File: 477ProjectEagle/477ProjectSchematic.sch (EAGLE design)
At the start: 66 parts, among them J1 POWER_JACKPTH, Q1 AO4419, X1 22-23-2051, X10 22-23-2041, X2 XRJK-S-01-6-6-0-2G2-NO

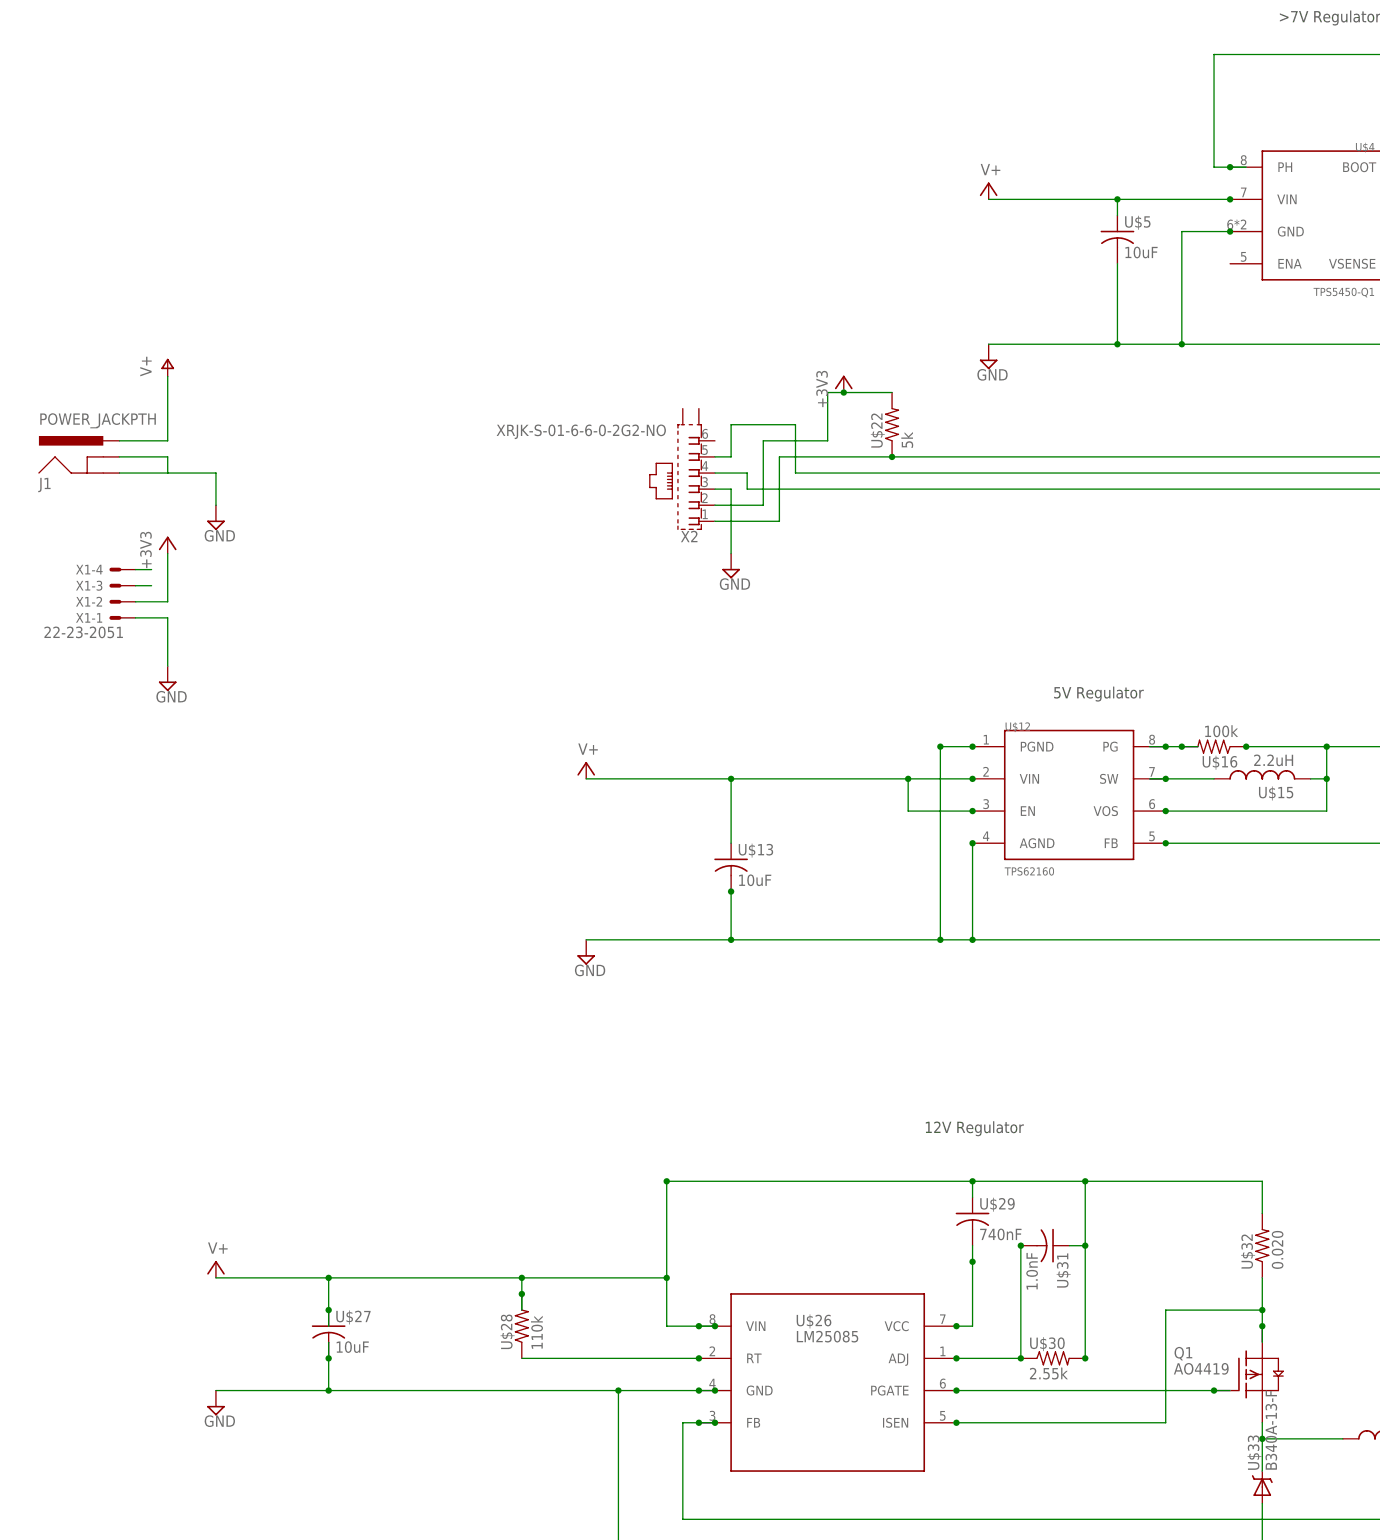
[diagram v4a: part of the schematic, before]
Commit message: started main PCB layout - 12V supply done
Started the PCB layout. Got the 12 volt power supply circuit done. We
only have the Light version of eagle so I couldn't actually make the PCB
the right size.
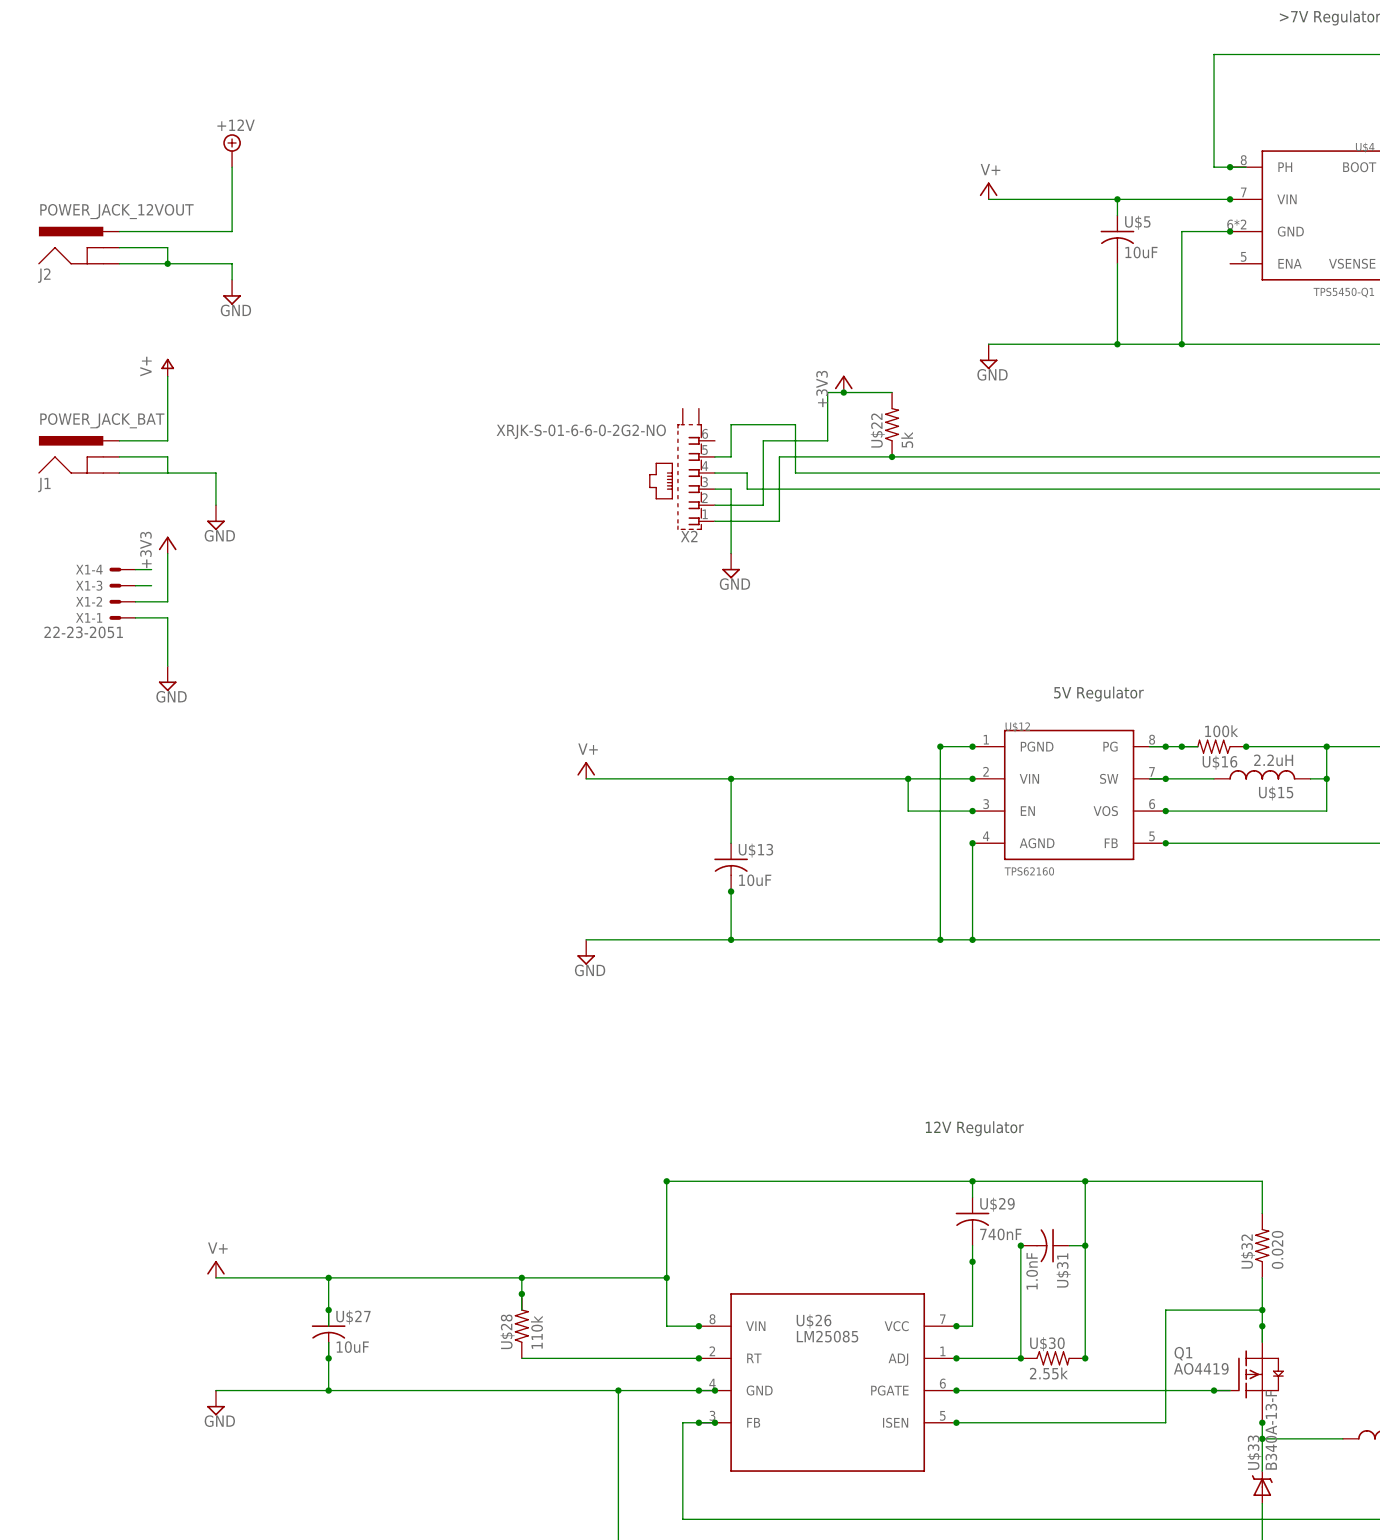
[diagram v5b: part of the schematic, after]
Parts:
- added J2: POWER_JACK_12VOUT, SparkFun-Connectors:POWER_JACKPTH
- J1: value POWER_JACKPTH -> POWER_JACK_BAT
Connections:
- net +12V: now also J2.PWR
- net GND: now also J2.GND, J2.GNDBREAK
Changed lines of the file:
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@@
 <part name="SUPPLY43" library="supply2" deviceset="V+" device=""/>
 <part name="+3V7" library="supply1" deviceset="+3V3" device=""/>
-<part name="J1" library="SparkFun-Connectors" deviceset="POWER_JACK" device="PTH"/>
+<part name="J1" library="SparkFun-Connectors" deviceset="POWER_JACK" device="PTH" value="POWER_JACK_BAT"/>
 <part name="P+1" library="supply1" deviceset="V+" device=""/>
 <part name="SUPPLY44" library="supply2" deviceset="GND" device=""/>
@@
 <part name="U$49" library="MinotaurParts" deviceset="C-US-1206" device="" value="10uF"/>
 <part name="SUPPLY48" library="supply2" deviceset="GND" device=""/>
+<part name="J2" library="SparkFun-Connectors" deviceset="POWER_JACK" device="PTH" value="POWER_JACK_12VOUT"/>
+<part name="SUPPLY49" library="supply2" deviceset="GND" device=""/>
+<part name="SUPPLY50" library="supply2" deviceset="+12V" device=""/>
 </parts>
 <sheets>
@@
 <instance part="U$49" gate="G$1" x="-172.72" y="-83.82"/>
 <instance part="SUPPLY48" gate="GND" x="-152.4" y="-93.98"/>
+<instance part="J2" gate="G$1" x="-436.88" y="73.66"/>
+<instance part="SUPPLY49" gate="GND" x="-416.56" y="71.12"/>
+<instance part="SUPPLY50" gate="+12V" x="-416.56" y="93.98"/>
 </instances>
 <busses>
@@
 <wire x1="-254" y1="-109.22" x2="-241.3" y2="-109.22" width="0.1524" layer="91"/>
 <junction x="-254" y="-109.22"/>
+<junction x="-254" y="-106.68"/>
 </segment>
 </net>
@@
 <junction x="-172.72" y="-88.9"/>
 </segment>
+<segment>
+<pinref part="J2" gate="G$1" pin="GNDBREAK"/>
+<wire x1="-434.34" y1="78.74" x2="-426.72" y2="78.74" width="0.1524" layer="91"/>
+<wire x1="-426.72" y1="78.74" x2="-426.72" y2="76.2" width="0.1524" layer="91"/>
+<pinref part="J2" gate="G$1" pin="GND"/>
+<wire x1="-426.72" y1="76.2" x2="-434.34" y2="76.2" width="0.1524" layer="91"/>
+<wire x1="-426.72" y1="76.2" x2="-416.56" y2="76.2" width="0.1524" layer="91"/>
+<wire x1="-416.56" y1="76.2" x2="-416.56" y2="73.66" width="0.1524" layer="91"/>
+<pinref part="SUPPLY49" gate="GND" pin="GND"/>
+<junction x="-426.72" y="76.2"/>
+</segment>
 </net>
 <net name="N$16" class="0">
@@
 <junction x="-175.26" y="-109.22"/>
 </segment>
+<segment>
+<pinref part="J2" gate="G$1" pin="PWR"/>
+<wire x1="-434.34" y1="81.28" x2="-416.56" y2="81.28" width="0.1524" layer="91"/>
+<wire x1="-416.56" y1="81.28" x2="-416.56" y2="91.44" width="0.1524" layer="91"/>
+<pinref part="SUPPLY50" gate="+12V" pin="+12V"/>
+</segment>
 </net>
 <net name="N$15" class="0">
@@
 <wire x1="-347.98" y1="-83.82" x2="-347.98" y2="-91.44" width="0.1524" layer="91"/>
 <wire x1="-347.98" y1="-91.44" x2="-342.9" y2="-91.44" width="0.1524" layer="91"/>
-<wire x1="-342.9" y1="-91.44" x2="-340.36" y2="-91.44" width="0.1524" layer="91"/>
 <wire x1="-370.84" y1="-88.9" x2="-370.84" y2="-86.36" width="0.1524" layer="91"/>
 <wire x1="-370.84" y1="-86.36" x2="-370.84" y2="-83.82" width="0.1524" layer="91"/>
@@
 <junction x="-281.94" y="-78.74"/>
 <junction x="-281.94" y="-96.52"/>
-<junction x="-340.36" y="-91.44"/>
 <pinref part="U$26" gate="G$1" pin="VIN"/>
-<junction x="-342.9" y="-91.44"/>
 <pinref part="U$27" gate="G$1" pin="1"/>
 <junction x="-401.32" y="-88.9"/>
@@
 <junction x="-401.32" y="-83.82"/>
 <pinref part="SUPPLY43" gate="1" pin="V+"/>
-</segment>
-<segment>
+<junction x="-342.9" y="-91.44"/>
+</segment>
+<segment>

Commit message: More work on main PCB
Fixed some trace sizes on 12V power supply. Fixed some library
components to be the right size (Cout for the 7V power supply). Started
laying out 7V power supply circuit
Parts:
- renumbered U$10 to D1_7, U$11 to COUT7, U$27 to CIN12, U$28 to RT12, U$29 to CVCC12, U$30 to RAJ12, U$31 to CADJ12, U$32 to RSNS12, U$33 to D1_12, U$34 to L1_12, U$38 to COUT12, U$5 to CIN7, U$6 to CBOOT7, U$7 to L1_7
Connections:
- net N$59: now also SV4.8
- net N$68: now also SV4.9
- net N$69: now also SV4.7
- net N$74: now also SV4.2
- net N$75: now also SV4.1

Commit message: Scott from lab -- worked on main PCB
Got all of the power supply circuits hooked up. Need to review them a
little bit more to make sure all traces are large enough etc...The board
is now 4 inches by 5 inches. That seems to be big enough
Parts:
- renumbered U$13 to CIN5, U$14 to COUT5, U$15 to L1_5, U$17 to R1_5, U$18 to R2_5
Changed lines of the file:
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@@
 <part name="D1_7" library="MinotaurParts" deviceset="B340A-13-F" device=""/>
 <part name="U$12" library="MinotaurParts" deviceset="TPS62160" device=""/>
-<part name="U$13" library="MinotaurParts" deviceset="C-US-1206" device="" value="10uF"/>
-<part name="U$14" library="MinotaurParts" deviceset="C-US-1206" device="" value="22uF"/>
+<part name="CIN5" library="MinotaurParts" deviceset="C-US-1206" device="" value="10uF"/>
+<part name="COUT5" library="MinotaurParts" deviceset="C-US-1206" device="" value="22uF"/>
 <part name="U$16" library="MinotaurParts" deviceset="R-US" device="&quot;" value="100k"/>
-<part name="U$17" library="MinotaurParts" deviceset="R-US" device="&quot;"/>
-<part name="U$18" library="MinotaurParts" deviceset="R-US" device="&quot;"/>
+<part name="R1_5" library="MinotaurParts" deviceset="R-US" device="&quot;"/>
+<part name="R2_5" library="MinotaurParts" deviceset="R-US" device="&quot;"/>
 <part name="U$26" library="MinotaurParts" deviceset="LM25085" device=""/>
 <part name="CIN12" library="MinotaurParts" deviceset="C-US-1210" device="" value="10uF"/>
@@
 <part name="SV4" library="con-lsta" deviceset="FE10-1" device=""/>
 <part name="+3V8" library="supply1" deviceset="+3V3" device=""/>
-<part name="U$15" library="MinotaurParts" deviceset="SDR0403" device="" value="2.2uH"/>
+<part name="L1_5" library="MinotaurParts" deviceset="SDR0403" device="" value="2.2uH"/>
 <part name="COUT7" library="MinotaurParts" deviceset="APXA100ARA271MJ80G" device="" value="270uF"/>
 <part name="CIN7" library="MinotaurParts" deviceset="C-US-1210" device="" value="10uF"/>
@@
 <instance part="D1_7" gate="G$1" x="-213.36" y="101.6" rot="MR90"/>
 <instance part="U$12" gate="G$1" x="-281.94" y="-12.7"/>
-<instance part="U$13" gate="G$1" x="-337.82" y="-17.78"/>
-<instance part="U$14" gate="G$1" x="-205.74" y="-7.62"/>
+<instance part="CIN5" gate="G$1" x="-337.82" y="-17.78"/>
+<instance part="COUT5" gate="G$1" x="-205.74" y="-7.62"/>
 <instance part="U$16" gate="G$1" x="-261.62" y="0" rot="R180"/>
-<instance part="U$17" gate="G$1" x="-226.06" y="-7.62" rot="R270"/>
-<instance part="U$18" gate="G$1" x="-226.06" y="-22.86" rot="R270"/>
+<instance part="R1_5" gate="G$1" x="-226.06" y="-7.62" rot="R270"/>
+<instance part="R2_5" gate="G$1" x="-226.06" y="-22.86" rot="R270"/>
 <instance part="U$26" gate="G$1" x="-322.58" y="-101.6"/>
 <instance part="CIN12" gate="G$1" x="-401.32" y="-91.44"/>
@@
 <instance part="SV4" gate="G$1" x="93.98" y="-50.8" rot="R90"/>
 <instance part="+3V8" gate="G$1" x="147.32" y="5.08"/>
-<instance part="U$15" gate="G$1" x="-254" y="-5.08" rot="R90"/>
+<instance part="L1_5" gate="G$1" x="-254" y="-5.08" rot="R90"/>
 <instance part="COUT7" gate="G$1" x="-175.26" y="73.66"/>
 <instance part="CIN7" gate="G$1" x="-276.86" y="81.28"/>
@@
 <junction x="-269.24" y="-5.08"/>
 <wire x1="-269.24" y1="-5.08" x2="-261.62" y2="-5.08" width="0.1524" layer="91"/>
-<pinref part="U$15" gate="G$1" pin="1"/>
+<pinref part="L1_5" gate="G$1" pin="1"/>
 </segment>
 </net>
@@
 <segment>
 <pinref part="U$12" gate="G$1" pin="FB"/>
-<pinref part="U$18" gate="G$1" pin="1"/>
+<pinref part="R2_5" gate="G$1" pin="1"/>
 <wire x1="-269.24" y1="-15.24" x2="-226.06" y2="-15.24" width="0.1524" layer="91"/>
 <wire x1="-226.06" y1="-15.24" x2="-226.06" y2="-17.78" width="0.1524" layer="91"/>
@@
 <junction x="-269.24" y="-15.24"/>
 <junction x="-226.06" y="-15.24"/>
-<pinref part="U$17" gate="G$1" pin="2"/>
+<pinref part="R1_5" gate="G$1" pin="2"/>
 <junction x="-226.06" y="-12.7"/>
 <wire x1="-226.06" y1="-12.7" x2="-226.06" y2="-10.16" width="0.1524" layer="91"/>
@@
 <segment>
 <pinref part="U$16" gate="G$1" pin="1"/>
-<pinref part="U$14" gate="G$1" pin="1"/>
+<pinref part="COUT5" gate="G$1" pin="1"/>
 <wire x1="-256.54" y1="0" x2="-243.84" y2="0" width="0.1524" layer="91"/>
 <wire x1="-243.84" y1="0" x2="-226.06" y2="0" width="0.1524" layer="91"/>
 <wire x1="-226.06" y1="0" x2="-205.74" y2="0" width="0.1524" layer="91"/>
 <wire x1="-205.74" y1="0" x2="-205.74" y2="-5.08" width="0.1524" layer="91"/>
-<pinref part="U$17" gate="G$1" pin="1"/>
+<pinref part="R1_5" gate="G$1" pin="1"/>
 <wire x1="-226.06" y1="-2.54" x2="-226.06" y2="0" width="0.1524" layer="91"/>
 <pinref part="U$12" gate="G$1" pin="VOS"/>
@@
 <pinref part="SUPPLY4" gate="+5V" pin="+5V"/>
 <junction x="-205.74" y="0"/>
-<pinref part="U$15" gate="G$1" pin="2"/>
+<pinref part="L1_5" gate="G$1" pin="2"/>
 <wire x1="-243.84" y1="-5.08" x2="-243.84" y2="0" width="0.1524" layer="91"/>
 <wire x1="-246.38" y1="-5.08" x2="-243.84" y2="-5.08" width="0.1524" layer="91"/>
@@
 </segment>
 <segment>
-<pinref part="U$13" gate="G$1" pin="2"/>
+<pinref part="CIN5" gate="G$1" pin="2"/>
 <junction x="-337.82" y="-22.86"/>
 <wire x1="-337.82" y1="-22.86" x2="-337.82" y2="-30.48" width="0.1524" layer="91"/>
-<pinref part="U$14" gate="G$1" pin="2"/>
+<pinref part="COUT5" gate="G$1" pin="2"/>
 <junction x="-205.74" y="-12.7"/>
 <wire x1="-205.74" y1="-12.7" x2="-205.74" y2="-30.48" width="0.1524" layer="91"/>
-<pinref part="U$18" gate="G$1" pin="2"/>
+<pinref part="R2_5" gate="G$1" pin="2"/>
 <junction x="-226.06" y="-27.94"/>
 <wire x1="-226.06" y1="-27.94" x2="-226.06" y2="-30.48" width="0.1524" layer="91"/>
@@
 <pinref part="SUPPLY42" gate="1" pin="V+"/>
 <wire x1="-360.68" y1="-5.08" x2="-337.82" y2="-5.08" width="0.1524" layer="91"/>
-<pinref part="U$13" gate="G$1" pin="1"/>
+<pinref part="CIN5" gate="G$1" pin="1"/>
 <wire x1="-337.82" y1="-5.08" x2="-309.88" y2="-5.08" width="0.1524" layer="91"/>
 <wire x1="-337.82" y1="-5.08" x2="-337.82" y2="-15.24" width="0.1524" layer="91"/>

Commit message: Continued work on main PCB
All components are in a rough position on the board. Everything just
needs to be connected now...
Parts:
- X10: value 22-23-2041 -> MOTORS
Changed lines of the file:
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@@
 <part name="U$3" library="MinotaurParts" deviceset="TXS0104E" device=""/>
 <part name="ENCODER" library="con-molex" deviceset="22-23-2021" device=""/>
-<part name="X10" library="con-molex" deviceset="22-23-2041" device=""/>
+<part name="X10" library="con-molex" deviceset="22-23-2041" device="" value="MOTORS"/>
 <part name="U$4" library="MinotaurParts" deviceset="TPS5450-Q1" device=""/>
 <part name="CBOOT7" library="MinotaurParts" deviceset="C-US-1206" device="" value="10nF"/>
@@
 <pinref part="SENSOR5" gate="-1" pin="S"/>
 <wire x1="2.54" y1="-96.52" x2="5.08" y2="-96.52" width="0.2032" layer="91"/>
-<junction x="2.54" y="-96.52"/>
 <pinref part="U$1" gate="A" pin="PMA7/C2OUT/AN9/RB9"/>
 <junction x="-78.74" y="-5.08"/>
@@
 <wire x1="-96.52" y1="-73.66" x2="-132.08" y2="-73.66" width="0.1524" layer="91"/>
 <junction x="-96.52" y="-73.66"/>
+<junction x="5.08" y="-96.52"/>
 </segment>
 </net>
@@
 <pinref part="X1" gate="-4" pin="S"/>
 <wire x1="-431.8" y1="27.94" x2="-429.26" y2="27.94" width="0.2032" layer="91"/>
+<wire x1="-429.26" y1="27.94" x2="-416.56" y2="27.94" width="0.1524" layer="91"/>
 </segment>
 </net>
@@
 <pinref part="X1" gate="-3" pin="S"/>
 <wire x1="-431.8" y1="25.4" x2="-429.26" y2="25.4" width="0.2032" layer="91"/>
-</segment>
-</net>
+<wire x1="-429.26" y1="25.4" x2="-416.56" y2="25.4" width="0.1524" layer="91"/>
+</segment>
+</net>
